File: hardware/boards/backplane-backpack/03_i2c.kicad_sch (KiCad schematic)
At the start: 15 parts, among them J3 I2C CH0 (TBD), J4 I2C CH1 (TBD), J5 I2C CH2 (TBD), J6 I2C CH3 (TBD), J7 I2C CH4 (TBD), J8 I2C CH5 (TBD), U2 TCA9548APWR

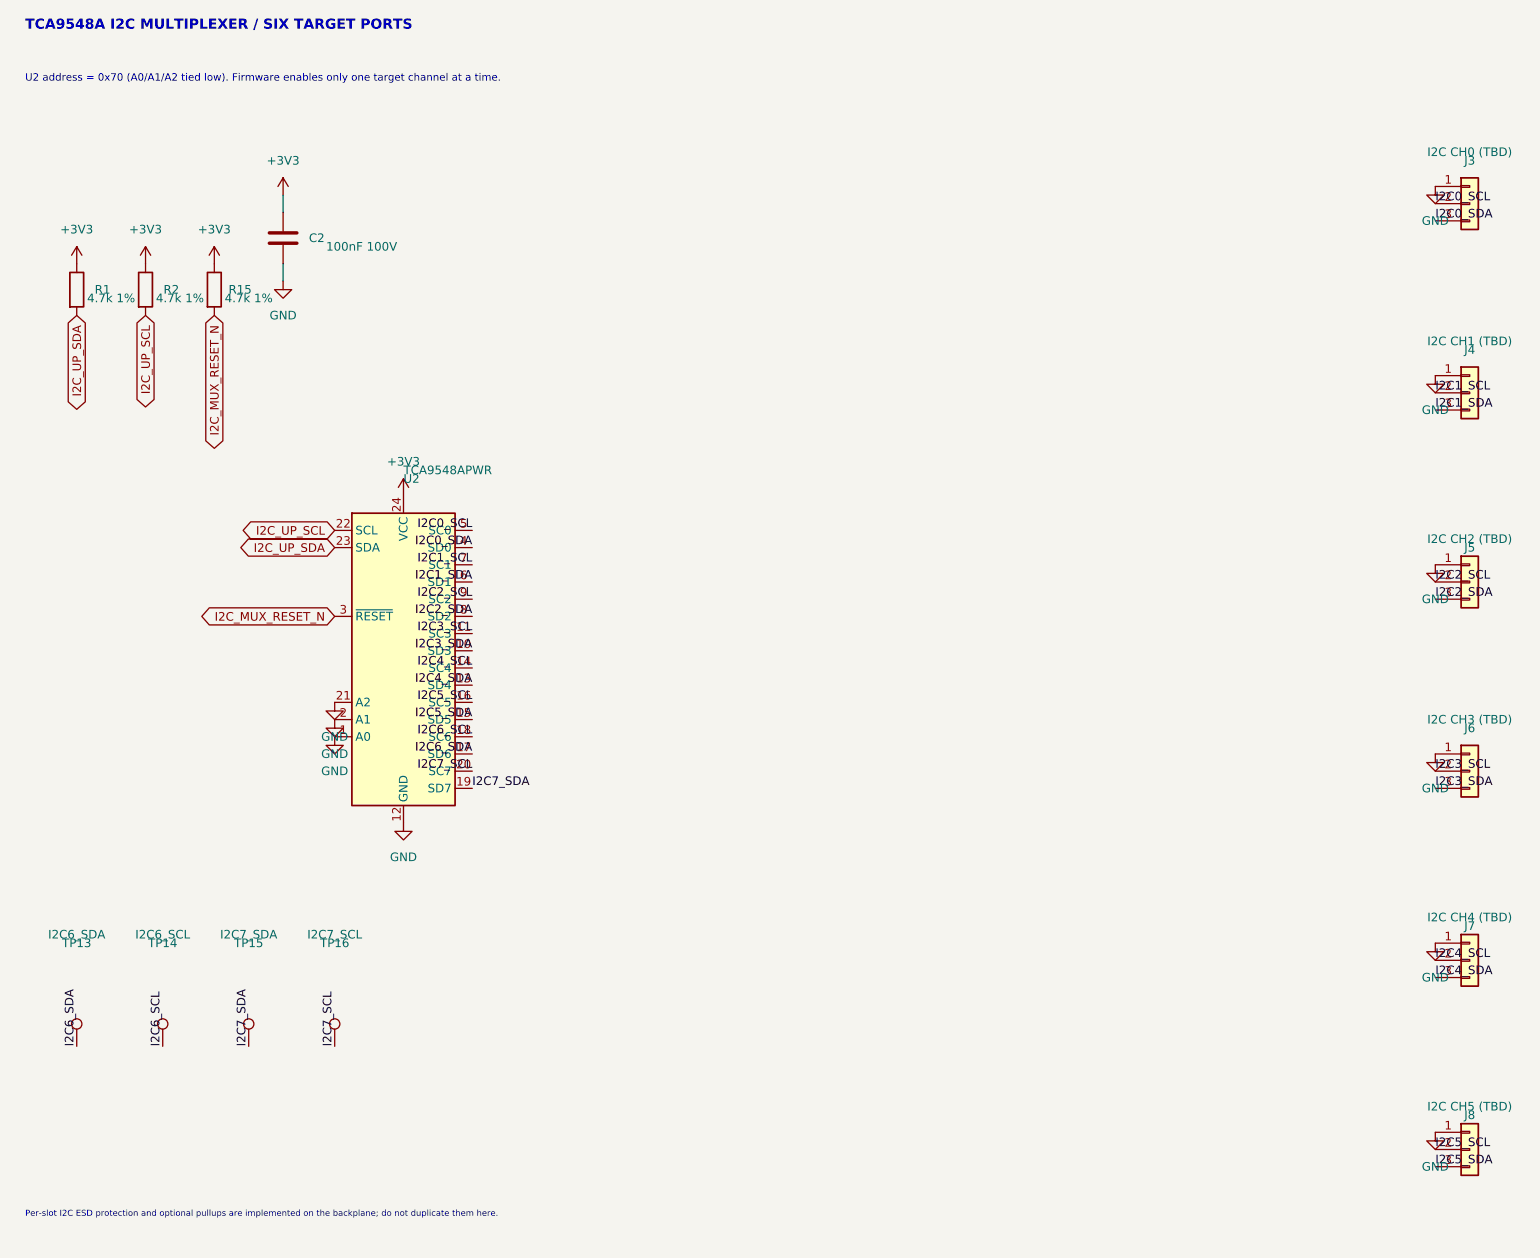
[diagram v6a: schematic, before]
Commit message: refactor: route backpack I2C through backplane mate
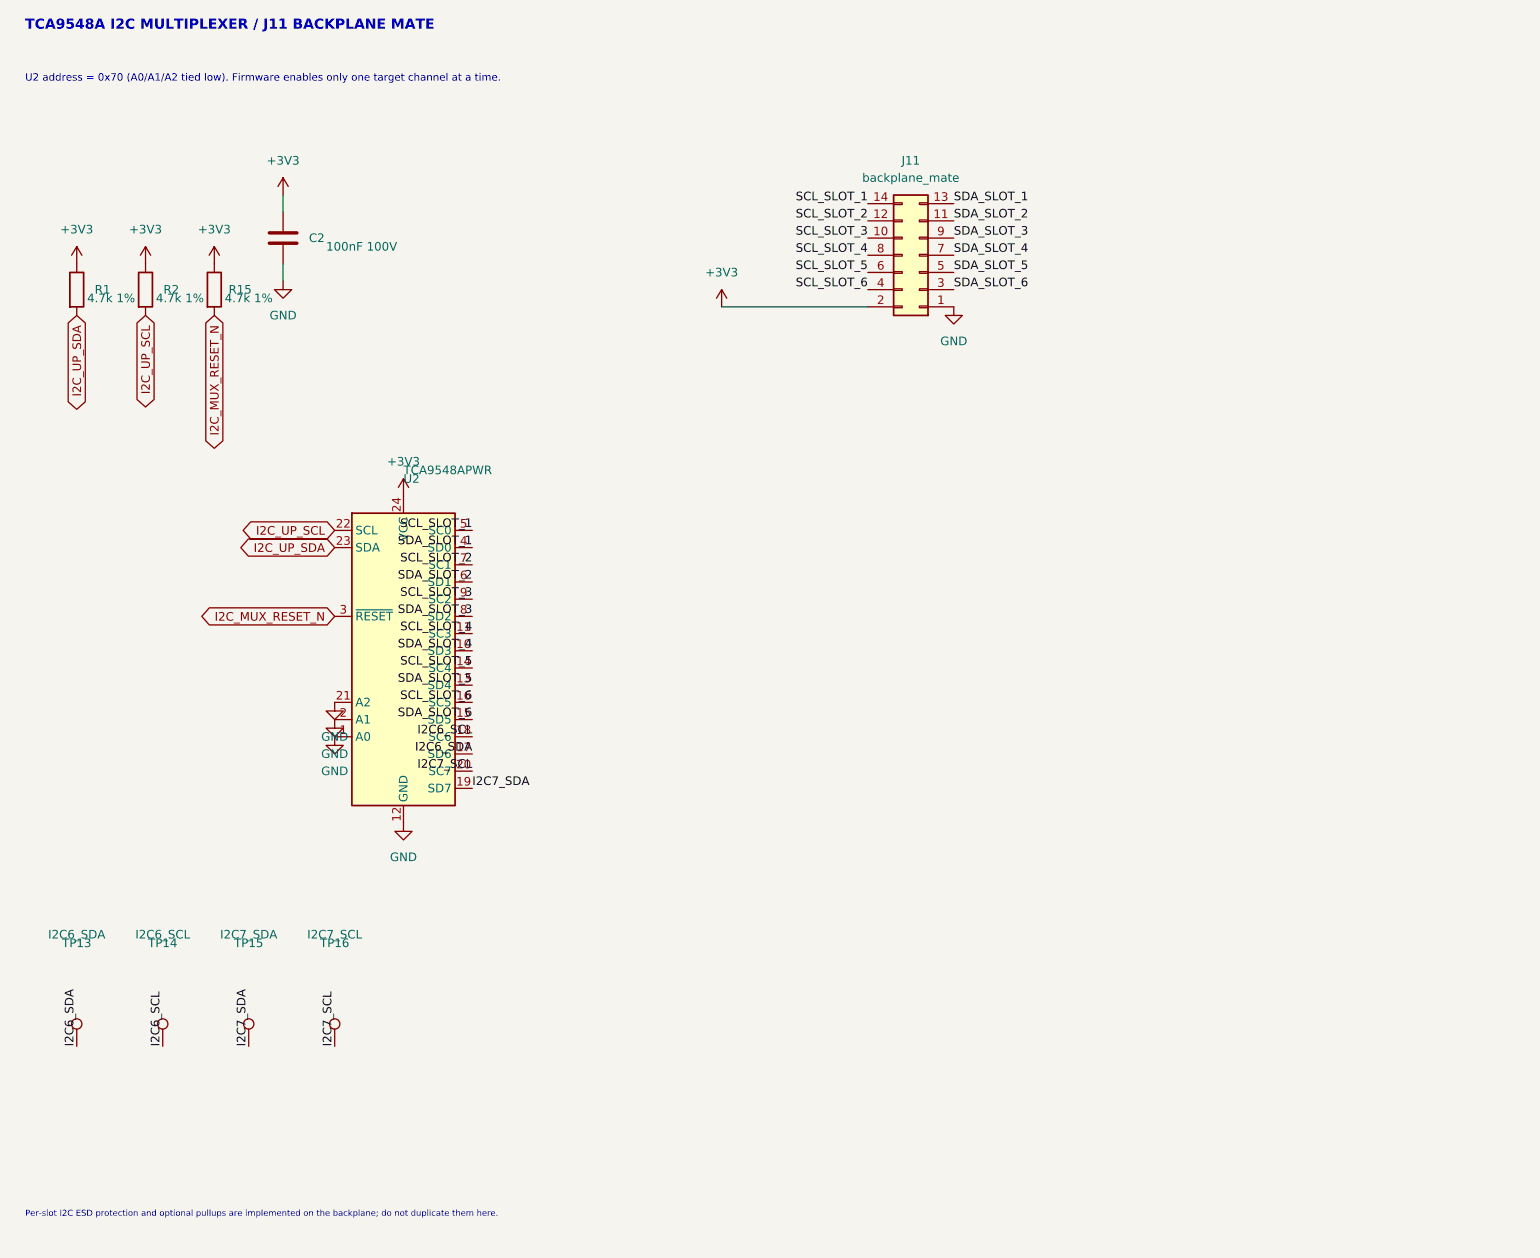
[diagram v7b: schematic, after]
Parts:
- removed J3: I2C CH0 (TBD), symbol Connector_Generic:Conn_01x03
- removed J4: I2C CH1 (TBD), symbol Connector_Generic:Conn_01x03
- removed J5: I2C CH2 (TBD), symbol Connector_Generic:Conn_01x03
- removed J6: I2C CH3 (TBD), symbol Connector_Generic:Conn_01x03
- removed J7: I2C CH4 (TBD), symbol Connector_Generic:Conn_01x03
- removed J8: I2C CH5 (TBD), symbol Connector_Generic:Conn_01x03
- added J11: backplane_mate, Connector_PinSocket_1.00mm:PinSocket_2x07_P1.00mm_Vertical_SMD, symbol Connector_Generic:Conn_02x07_Odd_Even
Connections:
- net +3V3: now also J11.2 (Pin_2)
- net GND: now also J11.1 (Pin_1)
- net I2C0_SCL renamed SCL_SLOT_1
- net SCL_SLOT_1: now also J11.14 (Pin_14)
- net I2C0_SDA renamed SDA_SLOT_1
- net SDA_SLOT_1: now also J11.13 (Pin_13)
- net I2C1_SCL renamed SCL_SLOT_2
- net SCL_SLOT_2: now also J11.12 (Pin_12)
- net I2C1_SDA renamed SDA_SLOT_2
- net SDA_SLOT_2: now also J11.11 (Pin_11)
- net I2C2_SCL renamed SCL_SLOT_3
- net SCL_SLOT_3: now also J11.10 (Pin_10)
- net I2C2_SDA renamed SDA_SLOT_3
- net SDA_SLOT_3: now also J11.9 (Pin_9)
- net I2C3_SCL renamed SCL_SLOT_4
- net SCL_SLOT_4: now also J11.8 (Pin_8)
- net I2C3_SDA renamed SDA_SLOT_4
- net SDA_SLOT_4: now also J11.7 (Pin_7)
- net I2C4_SCL renamed SCL_SLOT_5
- net SCL_SLOT_5: now also J11.6 (Pin_6)
- net I2C4_SDA renamed SDA_SLOT_5
- net SDA_SLOT_5: now also J11.5 (Pin_5)
- net I2C5_SCL renamed SCL_SLOT_6
- net SCL_SLOT_6: now also J11.4 (Pin_4)
- net I2C5_SDA renamed SDA_SLOT_6
- net SDA_SLOT_6: now also J11.3 (Pin_3)
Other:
- note added: "TCA9548A I2C MULTIPLEXER / J11 BACKPLANE MATE"
- note removed: "TCA9548A I2C MULTIPLEXER / SIX TARGET PORTS"

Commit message: chore: checkpoint current design changes
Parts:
- added JP1: A0_ADDR, Jumper:SolderJumper-3_P1.3mm_Bridged12_Pad1.0x1.5mm, symbol Jumper:SolderJumper_3_Bridged12
- added JP2: A1_ADDR, Jumper:SolderJumper-3_P1.3mm_Bridged12_Pad1.0x1.5mm, symbol Jumper:SolderJumper_3_Bridged12
- added JP3: A2_ADDR, Jumper:SolderJumper-3_P1.3mm_Bridged12_Pad1.0x1.5mm, symbol Jumper:SolderJumper_3_Bridged12
- TP14: value I2C6_SCL -> I2C6_SDA
- TP15: value I2C7_SDA -> I2C6_SDA
- TP16: value I2C7_SCL -> I2C6_SDA
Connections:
- net +3V3: now also JP1.3 (B), JP2.3 (B), JP3.3 (B)
- net GND: now also JP1.1 (A), JP2.1 (A), JP3.1 (A); no longer U2.1 (A0), U2.2 (A1), U2.21 (A2)
- net I2C_MUX_RESET_N: now also R1.2; no longer R15.2
- net I2C_UP_SCL: now also R15.2; no longer R2.2
- net I2C_UP_SDA: now also R2.2; no longer R1.2
- net I2C6_SCL: no longer names the net of TP14.1
- net I2C6_SCL: now also U2.17 (SD6); no longer U2.18 (SC6)
- net I2C6_SDA: no longer names the net of TP13.1
- net I2C6_SDA: now also U2.18 (SC6); no longer U2.17 (SD6)
- net I2C7_SCL: no longer names the net of TP16.1
- net I2C7_SCL: now also U2.19 (SD7); no longer U2.20 (SC7)
- net I2C7_SDA: no longer names the net of TP15.1
- net I2C7_SDA: now also U2.20 (SC7); no longer U2.19 (SD7)
- new net TCA9548A_A0: JP1.2 (C), U2.1 (A0)
- new net TCA9548A_A1: JP2.2 (C), U2.2 (A1)
- new net TCA9548A_A2: JP3.2 (C), U2.21 (A2)
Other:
- note added: "TCA9548A: JP1-JP3 default A0/A1/A2 low for 0x70; cut 1-2 and bridge 1-3 to set a bit high."
- note removed: "U2 address = 0x70 (A0/A1/A2 tied low). Firmware enables only one target channel at a time."
- moved on the sheet: C2, R1, R15, R2, TP13
